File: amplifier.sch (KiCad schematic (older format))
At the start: 15 parts, among them J2 J_3.5mm_jack_SJ1-3523N, Q1 Q_IRFZ44NPBF_N-Channel_Infine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, Q2 Q_IRFZ44NPBF_N-Channel_Infine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, U4 U_LM393N_NOPB, U5 U_TC4427M_Microchip

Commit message: changed vu meter resistor value's
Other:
- note removed: "Add decoupling?"
- note removed: "add bandpass filter for\n10h to 40khz"
- note removed: "add offset voltage \nto input signal"
- note removed: "improve switiching add snubbing\n"
- note removed: "square wave - PWM output"
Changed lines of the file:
@@
 EESchema Schematic File Version 4
-LIBS:versterker-cache
 EELAYER 30 0
 EELAYER END
@@
 Text HLabel 4700 2600 0    50   Input ~ 0
 Triangle_wave
-Text Notes 5000 3250 0    50   ~ 0
-square wave - PWM output
-Text Notes 3650 3550 0    50   ~ 0
-add bandpass filter for\n10h to 40khz
 $Comp
 L Main_Library:U_TC4427M_Microchip U5
@@
 Amplifier_output
 Connection ~ 7600 2100
-Text Notes 5050 2500 0    50   ~ 0
-Add decoupling?
-Text Notes 8750 3350 0    50   ~ 0
-improve switiching add snubbing\n
-Text Notes 3200 3100 0    50   ~ 0
-add offset voltage \nto input signal
 $Comp
 L Main_Library:U_LM393N_NOPB U4

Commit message: added raspberry pi hat pcb outline and layout
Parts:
- removed R8, R9: R_100K_0603, MAIN_PCB_LIB:R_0603, symbol Main_Library:R_100K_0603
- added R10, R13, R14, R4, R5: R_10K_0603, MAIN_PCB_LIB:R_0603, symbol Main_Library:R_10K_0603
- added R11: R_1K5_0603, MAIN_PCB_LIB:R_0603, symbol Main_Library:R_1K5_0603
- added R12: R_60.4K_0603, MAIN_PCB_LIB:R_0603, symbol Main_Library:R_60.4K_0603
- added R6: R_10K_Potmeter, MAIN_PCB_LIB:R_TH_POT_P160series, symbol Main_Library:R_10K_Potmeter
- added R9: R_20K_0603, MAIN_PCB_LIB:R_0603, symbol Main_Library:R_20K_0603
- added U2: U_LM358AP_TI_DIP, MAIN_PCB_LIB:U_LM358AP_TI_DIP, symbol Main_Library:U_LM358AP_TI_DIP
- renumbered C3 to C2, C4 to C3, C5 to C4, C6 to C5, C7 to C6, R6 to R7, R7 to R8, U4 to U3, U5 to U4
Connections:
- net labels added: 9V
- net labels removed: VIN
- wire segments 29 -> 36
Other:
- moved on the sheet: C2, C3, C4, C5, C6, J2, Q1, Q2, R7, R8, U3A, U3B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

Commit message: changed everything to 9V and changed inductor to match one in stock
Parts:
- removed L1: L_22uH_8095_WU-TI, MAIN_PCB_LIB:L_WE-TI_8095Series, symbol Main_Library:L_22uH_8095_WU-TI
- added J3: J_2_screwterminal_2.54_282834-2, MAIN_PCB_LIB:J_2_screwterminal_2.54, symbol Main_Library:J_2_screwterminal_2.54_282834-2
- added L1: L_22uH_RFS1113_coilcraft_TH, MAIN_PCB_LIB:L_RFS1113_coilcraft, symbol Main_Library:L_22uH_RFS1113_coilcraft_TH
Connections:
- net labels removed: Amplifier_output
- wire segments 36 -> 37
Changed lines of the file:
@@
 $Descr A4 11693 8268
 encoding utf-8
-Sheet 3 5
+Sheet 2 4
 Title ""
 Date ""
@@
 	0    -1   -1   0
 $EndComp
-Text HLabel 5500 2200 1    50   Input ~ 0
-5V
 Wire Wire Line
 	5500 2200 5500 2450
@@
 F 3 "" H 6660 2890 50  0001 C CNN
 	1    6750 2950
-	1    0    0    -1
-$EndComp
-$Comp
-L Main_Library:5V #PWR03
-U 1 1 61693B59
-P 5700 2450
-F 0 "#PWR03" H 5450 2550 50  0001 C CNN
-F 1 "5V" H 5700 2625 50  0000 C CNN
-F 2 "" H 5700 2600 50  0001 C CNN
-F 3 "" H 5700 2600 50  0001 C CNN
-	1    5700 2450
-	1    0    0    -1
-$EndComp
-Wire Wire Line
-	5500 2450 5700 2450
-$Comp
-L Main_Library:5V #PWR06
-U 1 1 61694913
-P 8100 2150
-F 0 "#PWR06" H 7850 2250 50  0001 C CNN
-F 1 "5V" H 8100 2325 50  0000 C CNN
-F 2 "" H 8100 2300 50  0001 C CNN
-F 3 "" H 8100 2300 50  0001 C CNN
-	1    8100 2150
 	1    0    0    -1
 $EndComp
@@
 $EndComp
 Connection ~ 3500 2750
-$Comp
-L Main_Library:5V #PWR02
-U 1 1 616E25EA
-P 5500 3500
-F 0 "#PWR02" H 5250 3600 50  0001 C CNN
-F 1 "5V" H 5500 3675 50  0000 C CNN
-F 2 "" H 5500 3650 50  0001 C CNN
-F 3 "" H 5500 3650 50  0001 C CNN
-	1    5500 3500
-	1    0    0    -1
-$EndComp
 Text HLabel 5200 3900 0    50   Input ~ 0
 Triangle_wave
@@
 Wire Wire Line
 	9200 2700 9200 2850
-$Comp
-L Main_Library:L_22uH_8095_WU-TI L1
-U 1 1 61713D2D
-P 9550 2850
-F 0 "L1" H 9550 3065 50  0000 C CNN
-F 1 "L_22uH_8095_WU-TI" H 9450 3250 50  0001 C CNN
-F 2 "MAIN_PCB_LIB:L_WE-TI_8095Series" H 9400 3150 50  0001 C CNN
-F 3 "" H 9350 2900 50  0001 C CNN
-F 4 "22uH" H 9550 2974 50  0000 C CNN "Waarde"
-F 5 "710-7447720220" H 9600 3050 50  0001 C CNN "Mouser"
-	1    9550 2850
-	1    0    0    -1
-$EndComp
-Connection ~ 9800 2850
 Wire Wire Line
 	9200 2850 9300 2850
@@
 Wire Wire Line
 	9200 2850 9200 3000
-Text HLabel 10150 2850 2    50   Output ~ 0
-Amplifier_output
-Connection ~ 8100 2150
 $Comp
 L Main_Library:U_LM393N_NOPB U3
@@
 	1    0    0    -1
 $EndComp
-Connection ~ 5500 2450
 $Comp
 L Main_Library:U_LM358AP_TI_DIP U2
@@
 Wire Wire Line
 	9200 2100 9250 2100
-Text Label 4700 2550 0    50   ~ 0
-9V
 $Comp
 L Main_Library:R_10K_Potmeter R6
@@
 Wire Wire Line
 	6250 3800 6550 3800
-$Comp
-L Main_Library:5V #PWR04
-U 1 1 61B6073B
-P 6250 2450
-F 0 "#PWR04" H 6000 2550 50  0001 C CNN
-F 1 "5V" H 6250 2625 50  0000 C CNN
-F 2 "" H 6250 2600 50  0001 C CNN
-F 3 "" H 6250 2600 50  0001 C CNN
-	1    6250 2450
-	1    0    0    -1
-$EndComp
-$Comp
-L Main_Library:5V #PWR05
-U 1 1 61B61659
-P 6250 3500
-F 0 "#PWR05" H 6000 3600 50  0001 C CNN
-F 1 "5V" H 6250 3675 50  0000 C CNN
-F 2 "" H 6250 3650 50  0001 C CNN
-F 3 "" H 6250 3650 50  0001 C CNN
-	1    6250 3500
-	1    0    0    -1
-$EndComp
 Wire Wire Line
 	7550 2750 8900 2750
@@
 	2850 2600 2850 2500
 Connection ~ 2850 2500
+Text Label 6250 2450 0    50   ~ 0
+9V
+Text Label 6250 3500 0    50   ~ 0
+9V
+Text Label 8150 2150 0    50   ~ 0
+9V
+Wire Wire Line
+	8100 2150 8150 2150
+Wire Wire Line
+	5500 3500 5550 3500
+Text HLabel 5500 2200 1    50   Input ~ 0
+9V
+Text HLabel 5500 3500 1    50   Input ~ 0
+9V
+Text HLabel 4700 2550 1    50   Input ~ 0
+9V
+$Comp
+L Main_Library:J_2_screwterminal_2.54_282834-2 J3
+U 1 1 61B3AC0A
+P 10350 2950
+F 0 "J3" H 10407 3125 50  0000 C CNN
+F 1 "J_2_screwterminal_2.54_282834-2" H 10230 2685 50  0001 L BNN
+F 2 "MAIN_PCB_LIB:J_2_screwterminal_2.54" H 10345 3105 50  0001 L BNN
+F 3 "" H 10350 2950 50  0001 L BNN
+F 4 "2" H 10350 2950 50  0001 L BNN "Number_of_Positions"
+F 5 "2.54 mm[.1 in]" H 10345 3105 50  0001 L BNN "Centerline_Pitch"
+F 6 "Compliant with Exemptions" H 10345 3105 50  0001 L BNN "EU_RoHS_Compliance"
+F 7 "282834-2" H 10350 3095 50  0001 L BNN "Comment"
+F 8 "571-282834-2" H 10350 2950 50  0001 C CNN "Mouser"
+	1    10350 2950
+	-1   0    0    1
+$EndComp
+$Comp
+L Main_Library:GND #GND04
+U 1 1 61B44A08
+P 10150 2950
+F 0 "#GND04" H 9990 2930 50  0001 C CNN
+F 1 "GND" H 9990 2930 50  0001 C CNN
+F 2 "" H 10060 2890 50  0001 C CNN
+F 3 "" H 10060 2890 50  0001 C CNN
+	1    10150 2950
+	1    0    0    -1
+$EndComp
+$Comp
+L Main_Library:L_22uH_RFS1113_coilcraft_TH L1
+U 1 1 61B4E324
+P 9550 2850
+F 0 "L1" H 9550 3065 50  0000 C CNN
+F 1 "L_22uH_RFS1113_coilcraft_TH" H 9450 3250 50  0001 C CNN
+F 2 "MAIN_PCB_LIB:L_RFS1113_coilcraft" H 9400 3150 50  0001 C CNN
+F 3 "" H 9350 2900 50  0001 C CNN
+F 4 "22uH" H 9550 2974 50  0000 C CNN "Waarde"
+F 5 "994-RFS1113-223ME" H 9600 3050 50  0001 C CNN "Mouser"
+	1    9550 2850
+	1    0    0    -1
+$EndComp
+Connection ~ 9800 2850
 $EndSCHEMATC

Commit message: changed vu meter circuit
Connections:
- net labels added: pre-amp-ouput
- net labels removed: 5V
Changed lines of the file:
@@
-$EndComp
-$Comp
-L Main_Library:5V #PWR01
-U 1 1 61B13FEE
-P 4000 2950
-F 0 "#PWR01" H 3750 3050 50  0001 C CNN
-F 1 "5V" H 4000 3125 50  0000 C CNN
-F 2 "" H 4000 3100 50  0001 C CNN
-F 3 "" H 4000 3100 50  0001 C CNN
-	1    4000 2950
-	1    0    0    -1
 $EndComp
 $Comp
@@
 $EndComp
 Connection ~ 9800 2850
+Text HLabel 5000 2850 3    50   Output ~ 0
+pre-amp-ouput
+Text Label 4000 2950 0    50   ~ 0
+9V
 $EndSCHEMATC

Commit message: routed pcb
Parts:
- added D15, D16: D_1N4148WS_SOD323F_ONSEMI, MAIN_PCB_LIB:D_1N4148_SOD-323F_ONSEMI, symbol Main_Library:D_1N4148WS_SOD323F_ONSEMI
- added R2: R_1K_0603, MAIN_PCB_LIB:R_0603, symbol Main_Library:R_1K_0603
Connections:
- net at R4.2, R5.1: now also R2.2; no longer R6.1
- new net: D15.C, D16.A, R2.1, R6.1
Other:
- moved on the sheet: C2, C3, J2, R10, R11, R12, R13, R14, R4, R5, R6, R7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

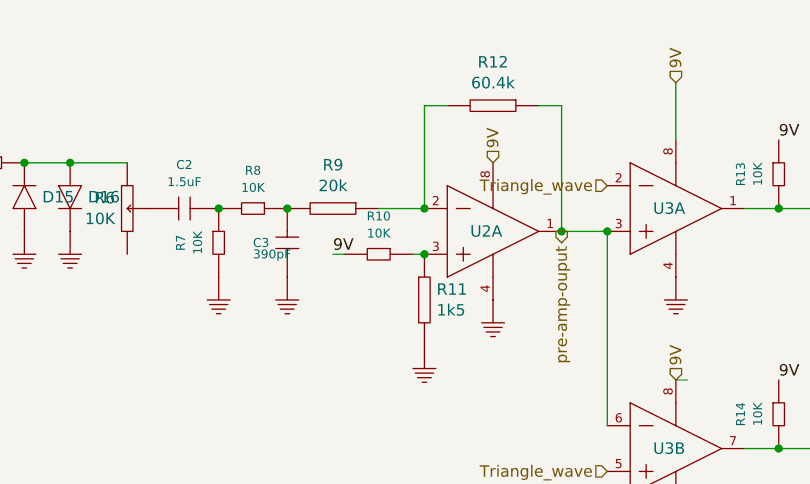
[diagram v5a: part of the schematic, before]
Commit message: made schematic changed based on testing
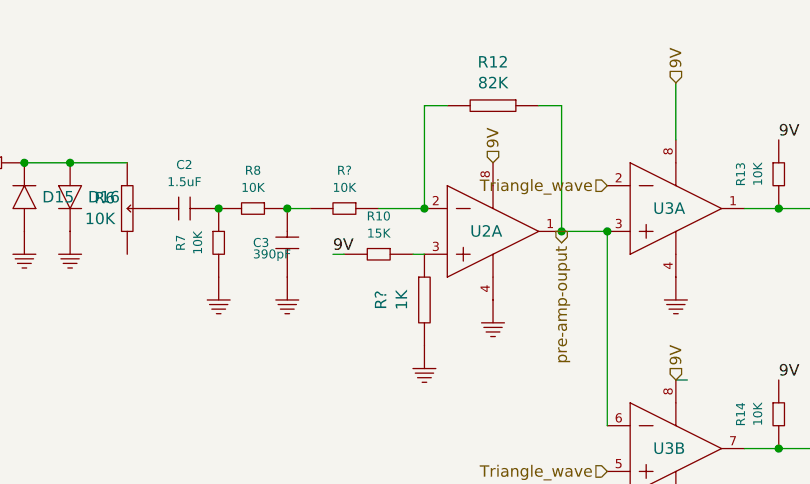
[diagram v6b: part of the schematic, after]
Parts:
- removed R11: R_1K5_0603, MAIN_PCB_LIB:R_0603, symbol Main_Library:R_1K5_0603
- removed R9: R_20K_0603, MAIN_PCB_LIB:R_0603, symbol Main_Library:R_20K_0603
- added R?: R_10K_0603, MAIN_PCB_LIB:R_0603, symbol Main_Library:R_10K_0603
- added R?: R_1K_0603, MAIN_PCB_LIB:R_0603, symbol Main_Library:R_1K_0603
- R10: Waarde 10K -> 15K
- R12: Waarde 60.4k -> 82K
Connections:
- net at C3.1, R8.1: now also R?.2
- net at R12.2, U2.2 (1IN-): now also R?.1
- net at R10.1, U2.3 (1IN+): now also R?.1
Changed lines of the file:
@@
 EESchema Schematic File Version 4
+LIBS:versterker-cache
 EELAYER 30 0
 EELAYER END
@@
 	1    0    0    -1
 $EndComp
-$Comp
-L Main_Library:R_20K_0603 R9
-U 1 1 61B0176D
-P 4450 2750
-F 0 "R9" V 4260 2750 50  0000 C CNN
-F 1 "R_20K_0603" H 4450 3200 50  0001 C CNN
-F 2 "MAIN_PCB_LIB:R_0603" H 4650 3270 50  0001 C CNN
-F 3 "" H 4400 2600 50  0001 C CNN
-F 4 "20k" V 4351 2750 50  0000 C CNN "Waarde"
-F 5 "603-RT0603FRE0720KL" H 4600 3350 50  0001 C CNN "Mouser"
-	1    4450 2750
-	0    1    1    0
-$EndComp
-Connection ~ 4250 2750
 Wire Wire Line
 	5450 2850 5650 2850
 Connection ~ 5650 2850
-Wire Wire Line
-	4650 2750 4850 2750
 Wire Wire Line
 	4850 2750 4850 2300
@@
 F 2 "MAIN_PCB_LIB:R_0603" H 5350 2820 50  0001 C CNN
 F 3 "" H 5100 2150 50  0001 C CNN
-F 4 "60.4k" V 5051 2300 50  0000 C CNN "Waarde"
+F 4 "82K" V 5051 2300 50  0000 C CNN "Waarde"
 F 5 "603-RT0603DRE0760K4L" H 5300 2900 50  0001 C CNN "Mouser"
 	1    5150 2300
@@
 F 2 "MAIN_PCB_LIB:R_0603" H 4650 3450 39  0001 C CNN
 F 3 "" H 4600 3100 39  0001 C CNN
-F 4 "10K" V 4559 2950 39  0000 C CNN "Waarde"
+F 4 "15K" V 4559 2950 39  0000 C CNN "Waarde"
 F 5 "YAG1236CT-ND" H 4650 3550 39  0001 C CNN "Digi-key"
 	1    4650 2950
 	0    1    1    0
-$EndComp
-$Comp
-L Main_Library:R_1K5_0603 R11
-U 1 1 61B1F191
-P 4850 3150
-F 0 "R11" H 4903 3196 50  0000 L CNN
-F 1 "R_1K5_0603" H 4850 3600 50  0001 C CNN
-F 2 "MAIN_PCB_LIB:R_0603" H 5050 3670 50  0001 C CNN
-F 3 "" H 4800 3000 50  0001 C CNN
-F 4 "1k5" H 4903 3105 50  0000 L CNN "Waarde"
-F 5 "603-RE0603FRE071K5L" H 5000 3750 50  0001 C CNN "Mouser"
-	1    4850 3150
-	1    0    0    -1
 $EndComp
 $Comp
@@
 Wire Wire Line
 	4800 2950 4850 2950
-Connection ~ 4850 2950
 Text HLabel 9200 2100 1    50   Input ~ 0
 9V
@@
 Wire Wire Line
 	3300 2550 3550 2550
+$Comp
+L Main_Library:R_10K_0603 R?
+U 1 1 61B43351
+P 4500 2750
+F 0 "R?" V 4334 2750 39  0000 C CNN
+F 1 "R_10K_0603" H 4450 3300 39  0001 C CNN
+F 2 "MAIN_PCB_LIB:R_0603" H 4500 3250 39  0001 C CNN
+F 3 "" H 4450 2900 39  0001 C CNN
+F 4 "10K" V 4409 2750 39  0000 C CNN "Waarde"
+F 5 "YAG1236CT-ND" H 4500 3350 39  0001 C CNN "Digi-key"
+	1    4500 2750
+	0    1    1    0
+$EndComp
+Wire Wire Line
+	4650 2750 4850 2750
+Wire Wire Line
+	4250 2750 4350 2750
+Connection ~ 4250 2750
+$Comp
+L Main_Library:R_1K_0603 R?
+U 1 1 61B46412
+P 4850 3150
+F 0 "R?" V 4660 3150 50  0000 C CNN
+F 1 "R_1K_0603" H 4850 3600 50  0001 C CNN
+F 2 "MAIN_PCB_LIB:R_0603" H 5050 3670 50  0001 C CNN
+F 3 "" H 4800 3000 50  0001 C CNN
+F 4 "1K" V 4751 3150 50  0000 C CNN "Waarde"
+F 5 "311-1.0KDDKR-ND" H 5000 3750 50  0001 C CNN "Digi-Key"
+	1    4850 3150
+	1    0    0    -1
+$EndComp
 $EndSCHEMATC

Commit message: no message
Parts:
- removed R10, R5, R?: R_10K_0603, MAIN_PCB_LIB:R_0603, symbol Main_Library:R_10K_0603
- removed R12: R_60.4K_0603, MAIN_PCB_LIB:R_0603, symbol Main_Library:R_60.4K_0603
- removed R?: R_1K_0603, MAIN_PCB_LIB:R_0603, symbol Main_Library:R_1K_0603
- added C8: C_680nF_TH_450V, MAIN_PCB_LIB:C_ECWFD_Panasonic, symbol Main_Library:C_680nF_TH_450V
- added L2: L_22uH_RFS1113_coilcraft_TH, MAIN_PCB_LIB:L_RFS1113_coilcraft, symbol Main_Library:L_22uH_RFS1113_coilcraft_TH
- added R3: R_20K_0603, MAIN_PCB_LIB:R_0603, symbol Main_Library:R_20K_0603
- added R5: R_2K_0603, MAIN_PCB_LIB:R_0603, symbol Main_Library:R_2K_0603
- added R9: R_60.4K_0603, MAIN_PCB_LIB:R_0603, symbol Main_Library:R_60.4K_0603
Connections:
- net 9V: now also R4.2
- net L_channel: now also J2.3, R2.2
- net pre-amp-ouput: now also R9.2
- net at C3.1, R8.1: now also R3.2
- net at C6.1, L1.2: now also L2.1; no longer J3.2
- net at U2.2 (1IN-): now also R3.1, R9.1
- net at U2.3 (1IN+): now also R4.1, R5.1
- removed net R_channel: J2.3, R4.1
- new net: C8.1, J3.2, L2.2
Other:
- moved on the sheet: J3

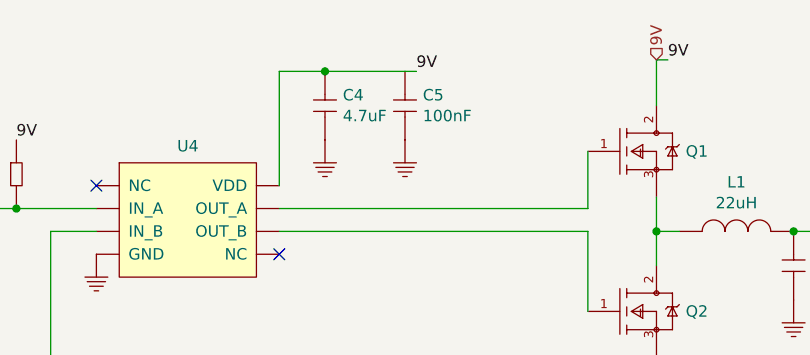
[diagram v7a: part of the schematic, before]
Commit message: changed partnumbers
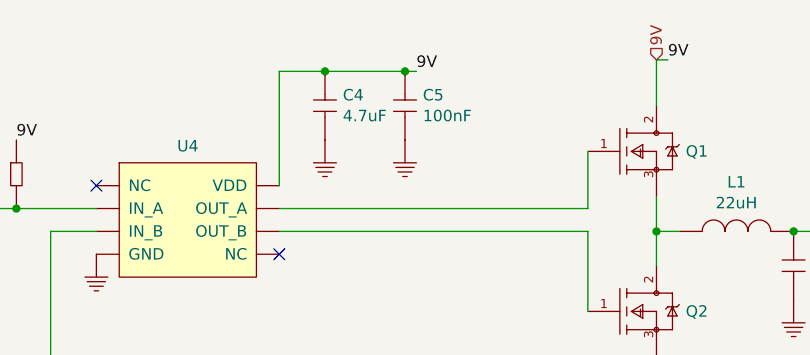
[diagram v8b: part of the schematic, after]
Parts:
- removed C5: C_100nF_0603_50V, MAIN_PCB_LIB:C_0603, symbol Main_Library:C_100nF_0603_50V
- added C5: C_100nF_0603_25V, MAIN_PCB_LIB:C_0603, symbol Main_Library:C_100nF_0603_25V
- C2: Digi-Key 445-5962-1-ND -> (none); Mouser (none) -> 810-C1608X5R1E155K
- C3: Digi-Key 399-1074-1-ND -> (none); Mouser (none) -> 80-C0603C391K5R
- C4: footprint MAIN_PCB_LIB:C_0603 -> Main_LIB:C_0603; Digi-Key 587-4321-1-ND -> (none); Mouser (none) -> 963-TMK107BBJ475KA-T
- J2: footprint MAIN_PCB_LIB:J_3.5mm_JACK_CUI_SJ1-3523N -> CUI_SJ1-3523N; MANUFACTURER CUI -> (none); Mouser (none) -> 490-SJ1-3523N; PARTREV 1.02 -> (none); STANDARD Manufacturer recommendation -> (none)
- Q1, Q2: Current - Continuous Drain 49A -> (none); Drain to Source Voltage 55V -> (none); FET Type N-Channel -> (none); Mouser (none) -> 942-IRFZ44NPBF; Rds On 17.5 mOhm -> (none); category Trans -> (none); digikey description N-Channel 55V 49A (Tc) 94W (Tc) Through Hole TO-220AB -> (none); digikey part number IRFZ44NPBF-ND -> (none); ipc land pattern name TO-220 -> (none); lead free yes -> (none); library id 28a2cf11992d899a -> (none); manufacturer Infineon Technologies AG -> (none); mouser part number 942-IRFZ44NPBF -> (none); package TO-220AB -> (none); rohs yes -> (none); temperature range high +175°C -> (none); temperature range low -55°C -> (none)
- R13, R14, R4, R7, R8: Digi-key YAG1236CT-ND -> (none); Mouser (none) -> 667-ERJ-UP3F1002V
- R2: Digi-Key 311-1.0KDDKR-ND -> (none); Mouser (none) -> 667-ERJ-PB3D1001V
- U2: Component Link 1 Description Manufacturer URL -> (none); Component Link 1 URL http://www.ti.com/ -> (none); Component Link 3 Description Package Specification -> (none); Component Link 3 URL http://www.ti.com/lit/ml/mpdi001b/mpdi001b.pdf -> (none); Datasheet Version SLOS068T, 04/2015 -> (none); Forward Current 20 mA -> (none); Forward Voltage 2 V -> (none); Height 1.1 mm -> (none); Illumination Colour Orange -> (none); Length 1.6 mm -> (none); Lens Style Diffused -> (none); Luminous Intensity 90 mcd -> (none); Max Operating Temperature 85 degC -> (none); Min Operating Temperature -55 degC -> (none); Mount Surface Mount -> (none); Mouser (none) -> 926-LM358N/NOPB; Nominal Vf 2 V -> (none); Package Description 8-Pin Double In-line Package, Body 9.59 x 6.35 mm, Pitch 2.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 -> (none); Package Quantity 3000 -> (none); Package Version 4040082/E, 04/2010 -> (none); Packaging Tape and Reel -> (none); Pins 2 -> (none); Power Rating 75 mW -> (none); Radiation Hardening No -> (none); Ro HSCompliant true -> (none); Viewing Angle 130 degrees -> (none); Width 0.8 mm -> (none); category IC -> (none); ciiva ids 13597420 -> (none); imported yes -> (none); library id 102746b87d6455a5 -> (none); manufacturer Texas Instruments -> (none); package P0008A -> (none); release date 1475053146 -> (none); vault revision 197138BC-30E5-4CB1-984F-D199D98786C8 -> (none)
- U3: Comp Type Amplifiers -> (none); Component Link 1 Description Datasheet URL -> (none); Component Link 1 URL http://www.ti.com/general/docs/lit/getliterature.tsp?generi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 -> (none); Mouser (none) -> 926-LM393N/NOPB; Package Description MDIP, .365 x .250 x .130in, 8 Lead, .100in Pitch -> (none); Package Reference P0008A -> (none); Package Top Marking NSUZXYTTE#*LM*393N -> (none); Pin Count 8 -> (none); Power Wise N -> (none); category IC -> (none); ciiva ids 1156860 -> (none); imported yes -> (none); library id 56c718e248e42434 -> (none); manufacturer TI National Semiconductor -> (none); package MS-001-BA -> (none); release date 1464069057 -> (none); rohs Yes -> (none); vault revision 5C587BB4-AF8A-4456-AC4A-BF04D6254C91 -> (none)
- U4: Mouser (none) -> 579-TC4427ACPA; mouser 579-TC4427ACPA -> (none)
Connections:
- net 9V: now also C5.1
